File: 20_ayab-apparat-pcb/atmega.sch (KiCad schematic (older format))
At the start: 35 parts, among them P7 CONN_3X2, P8 CONN_4, P9 CONN_2, SW1 SW_PUSH, U6 ATMEGA32U4-A, X1 16MHz, X2 USBMINI

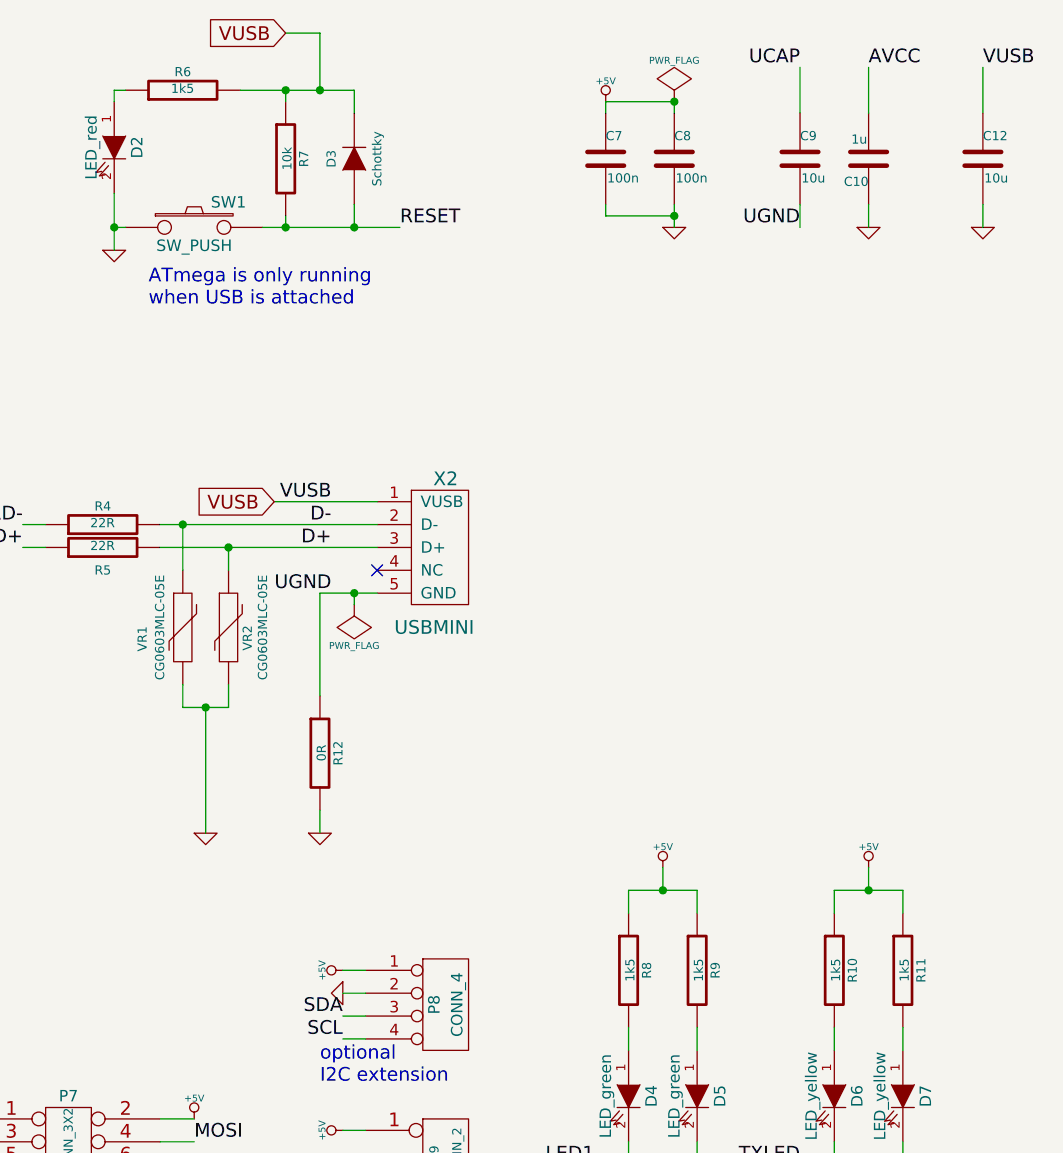
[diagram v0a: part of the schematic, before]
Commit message: fixed LED resistor value
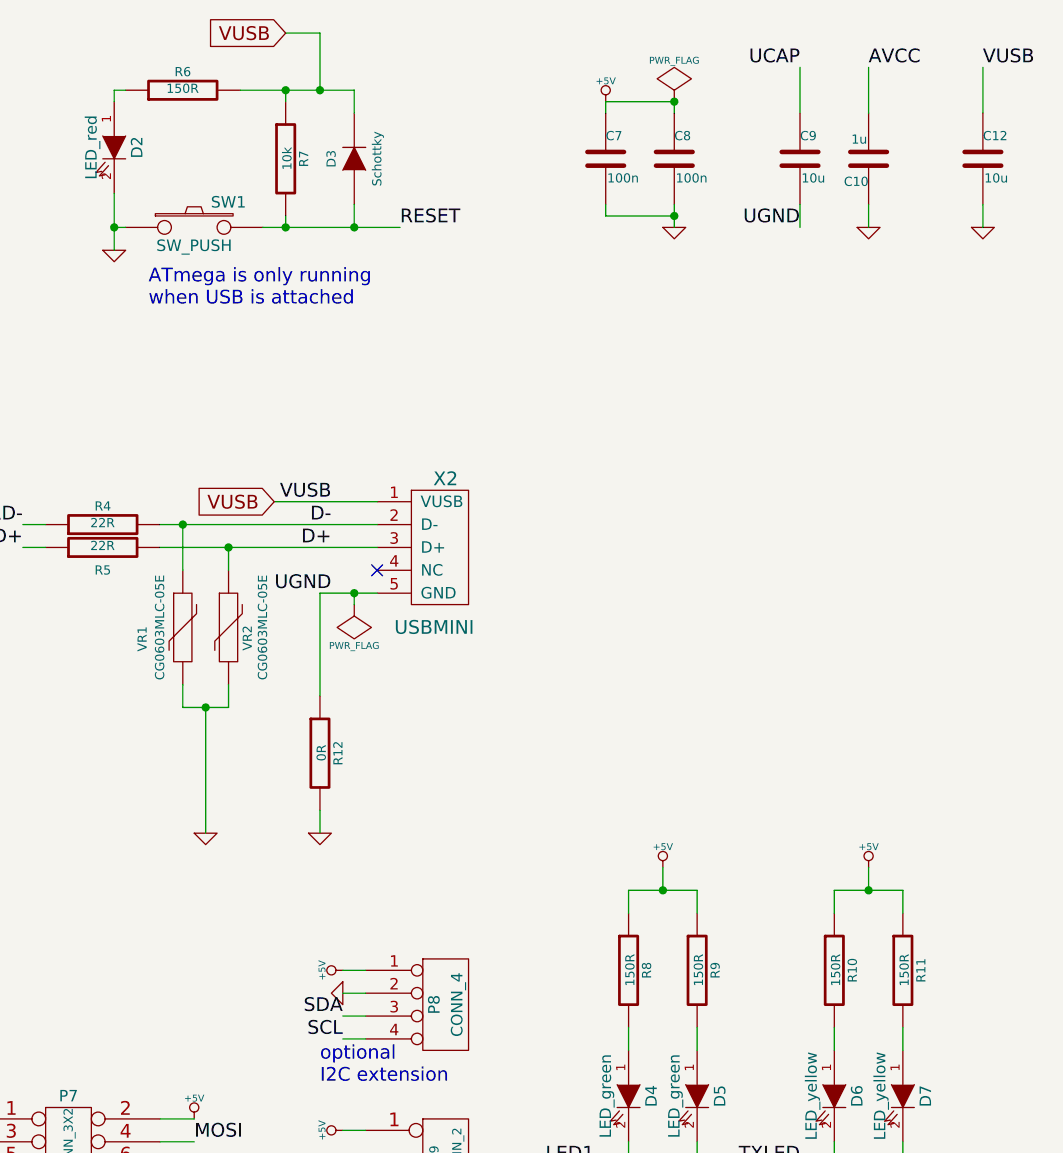
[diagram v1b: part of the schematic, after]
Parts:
- R10, R11, R6, R8, R9: value 1k5 -> 150R
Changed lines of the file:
@@
 OSC2
 $Comp
-L GND #PWR38
+L GND #PWR034
 U 1 1 52E8074E
 P 4750 1850
-F 0 "#PWR38" H 4750 1850 30  0001 C CNN
+F 0 "#PWR034" H 4750 1850 30  0001 C CNN
 F 1 "GND" H 4750 1780 30  0001 C CNN
 F 2 "" H 4750 1850 60  0000 C CNN
@@
 $EndComp
 $Comp
-L PWR_FLAG #FLG2
+L PWR_FLAG #FLG035
 U 1 1 52E8077D
 P 4750 1100
-F 0 "#FLG2" H 4750 1195 30  0001 C CNN
+F 0 "#FLG035" H 4750 1195 30  0001 C CNN
 F 1 "PWR_FLAG" H 4750 1280 30  0000 C CNN
 F 2 "" H 4750 1100 60  0000 C CNN
@@
 $EndComp
 $Comp
-L GND #PWR49
+L GND #PWR036
 U 1 1 52E80927
 P 9200 1700
-F 0 "#PWR49" H 9200 1700 30  0001 C CNN
+F 0 "#PWR036" H 9200 1700 30  0001 C CNN
 F 1 "GND" H 9200 1630 30  0001 C CNN
 F 2 "" H 9200 1700 60  0000 C CNN
@@
 $EndComp
 $Comp
-L PWR_FLAG #FLG4
+L PWR_FLAG #FLG037
 U 1 1 52E809A6
 P 9200 1150
-F 0 "#FLG4" H 9200 1245 30  0001 C CNN
+F 0 "#FLG037" H 9200 1245 30  0001 C CNN
 F 1 "PWR_FLAG" H 9200 1330 30  0000 C CNN
 F 2 "" H 9200 1150 60  0000 C CNN
@@
 $EndComp
 $Comp
-L GND #PWR34
+L GND #PWR038
 U 1 1 52E80AA1
 P 1450 5850
-F 0 "#PWR34" H 1450 5850 30  0001 C CNN
+F 0 "#PWR038" H 1450 5850 30  0001 C CNN
 F 1 "GND" H 1450 5780 30  0001 C CNN
 F 2 "" H 1450 5850 60  0000 C CNN
@@
 ISP
 $Comp
-L GND #PWR41
+L GND #PWR039
 U 1 1 52E80DFA
 P 7100 5850
-F 0 "#PWR41" H 7100 5850 30  0001 C CNN
+F 0 "#PWR039" H 7100 5850 30  0001 C CNN
 F 1 "GND" H 7100 5780 30  0001 C CNN
 F 2 "" H 7100 5850 60  0000 C CNN
@@
 MOSI
 $Comp
-L +5V #PWR40
+L +5V #PWR040
 U 1 1 52E80E45
 P 7100 5600
-F 0 "#PWR40" H 7100 5690 20  0001 C CNN
+F 0 "#PWR040" H 7100 5690 20  0001 C CNN
 F 1 "+5V" H 7100 5690 30  0000 C CNN
 F 2 "" H 7100 5600 60  0000 C CNN
@@
 P 7050 1100
 F 0 "R6" V 7130 1100 40  0000 C CNN
-F 1 "1k5" V 7057 1101 40  0000 C CNN
+F 1 "150R" V 7057 1101 40  0000 C CNN
 F 2 "" V 6980 1100 30  0000 C CNN
 F 3 "" H 7050 1100 30  0000 C CNN
@@
 $EndComp
 $Comp
-L GND #PWR39
+L GND #PWR041
 U 1 1 52E813A7
 P 6750 1800
-F 0 "#PWR39" H 6750 1800 30  0001 C CNN
+F 0 "#PWR041" H 6750 1800 30  0001 C CNN
 F 1 "GND" H 6750 1730 30  0001 C CNN
 F 2 "" H 6750 1800 60  0000 C CNN
@@
 $EndComp
 $Comp
-L +5V #PWR37
+L +5V #PWR042
 U 1 1 52E81906
 P 4350 3500
-F 0 "#PWR37" H 4350 3590 20  0001 C CNN
+F 0 "#PWR042" H 4350 3590 20  0001 C CNN
 F 1 "+5V" H 4350 3590 30  0000 C CNN
 F 2 "" H 4350 3500 60  0000 C CNN
@@
 $EndComp
 $Comp
-L +5V #PWR33
+L +5V #PWR043
 U 1 1 52E81C3C
 P 1300 5300
-F 0 "#PWR33" H 1300 5390 20  0001 C CNN
+F 0 "#PWR043" H 1300 5390 20  0001 C CNN
 F 1 "+5V" H 1300 5390 30  0000 C CNN
 F 2 "" H 1300 5300 60  0000 C CNN
@@
 RESET
 $Comp
-L GND #PWR35
+L GND #PWR044
 U 1 1 52E9637A
 P 2900 6200
-F 0 "#PWR35" H 2900 6200 30  0001 C CNN
+F 0 "#PWR044" H 2900 6200 30  0001 C CNN
 F 1 "GND" H 2900 6130 30  0001 C CNN
 F 2 "" H 2900 6200 60  0000 C CNN
@@
 $EndComp
 $Comp
-L GND #PWR42
+L GND #PWR045
 U 1 1 52E97A05
 P 7150 4350
-F 0 "#PWR42" H 7150 4350 30  0001 C CNN
+F 0 "#PWR045" H 7150 4350 30  0001 C CNN
 F 1 "GND" H 7150 4280 30  0001 C CNN
 F 2 "" H 7150 4350 60  0000 C CNN
@@
 $EndComp
 $Comp
-L GND #PWR50
+L GND #PWR046
 U 1 1 52E97015
 P 10050 1700
-F 0 "#PWR50" H 10050 1700 30  0001 C CNN
+F 0 "#PWR046" H 10050 1700 30  0001 C CNN
 F 1 "GND" H 10050 1630 30  0001 C CNN
 F 2 "" H 10050 1700 60  0000 C CNN
@@
 $EndComp
 $Comp
-L GND #PWR52
+L GND #PWR047
 U 1 1 52E972FE
 P 10550 1700
-F 0 "#PWR52" H 10550 1700 30  0001 C CNN
+F 0 "#PWR047" H 10550 1700 30  0001 C CNN
 F 1 "GND" H 10550 1630 30  0001 C CNN
 F 2 "" H 10550 1700 60  0000 C CNN
@@
 RXLED
 $Comp
-L +5V #PWR51
+L +5V #PWR048
 U 1 1 52E980C3
 P 10050 4500
-F 0 "#PWR51" H 10050 4590 20  0001 C CNN
+F 0 "#PWR048" H 10050 4590 20  0001 C CNN
 F 1 "+5V" H 10050 4590 30  0000 C CNN
 F 2 "" H 10050 4500 60  0000 C CNN
@@
 P 9900 4950
 F 0 "R10" V 9980 4950 40  0000 C CNN
-F 1 "1k5" V 9907 4951 40  0000 C CNN
+F 1 "150R" V 9907 4951 40  0000 C CNN
 F 2 "" V 9830 4950 30  0000 C CNN
 F 3 "" H 9900 4950 30  0000 C CNN
@@
 P 10200 4950
 F 0 "R11" V 10280 4950 40  0000 C CNN
-F 1 "1k5" V 10207 4951 40  0000 C CNN
+F 1 "150R" V 10207 4951 40  0000 C CNN
 F 2 "" V 10130 4950 30  0000 C CNN
 F 3 "" H 10200 4950 30  0000 C CNN
@@
 $EndComp
 $Comp
-L +5V #PWR46
+L +5V #PWR049
 U 1 1 52EA92E6
 P 7750 5650
-F 0 "#PWR46" H 7750 5740 20  0001 C CNN
+F 0 "#PWR049" H 7750 5740 20  0001 C CNN
 F 1 "+5V" H 7750 5740 30  0000 C CNN
 F 2 "" H 7750 5650 60  0000 C CNN
@@
 $EndComp
 $Comp
-L +5V #PWR44
+L +5V #PWR050
 U 1 1 52EA9766
 P 7750 4950
-F 0 "#PWR44" H 7750 5040 20  0001 C CNN
+F 0 "#PWR050" H 7750 5040 20  0001 C CNN
 F 1 "+5V" H 7750 5040 30  0000 C CNN
 F 2 "" H 7750 4950 60  0000 C CNN
@@
 $EndComp
 $Comp
-L GND #PWR45
+L GND #PWR051
 U 1 1 52EA977A
 P 7750 5050
-F 0 "#PWR45" H 7750 5050 30  0001 C CNN
+F 0 "#PWR051" H 7750 5050 30  0001 C CNN
 F 1 "GND" H 7750 4980 30  0001 C CNN
 F 2 "" H 7750 5050 60  0000 C CNN
@@
 LED2
 $Comp
-L +5V #PWR48
+L +5V #PWR052
 U 1 1 52EA9B0A
 P 9150 4500
-F 0 "#PWR48" H 9150 4590 20  0001 C CNN
+F 0 "#PWR052" H 9150 4590 20  0001 C CNN
 F 1 "+5V" H 9150 4590 30  0000 C CNN
 F 2 "" H 9150 4500 60  0000 C CNN
@@
 P 9000 4950
 F 0 "R8" V 9080 4950 40  0000 C CNN
-F 1 "1k5" V 9007 4951 40  0000 C CNN
+F 1 "150R" V 9007 4951 40  0000 C CNN
 F 2 "" V 8930 4950 30  0000 C CNN
 F 3 "" H 9000 4950 30  0000 C CNN
@@
 P 9300 4950
 F 0 "R9" V 9380 4950 40  0000 C CNN
-F 1 "1k5" V 9307 4951 40  0000 C CNN
+F 1 "150R" V 9307 4951 40  0000 C CNN
 F 2 "" V 9230 4950 30  0000 C CNN
 F 3 "" H 9300 4950 30  0000 C CNN
@@
 LED1
 $Comp
-L +5V #PWR36
+L +5V #PWR053
 U 1 1 52EAA0EE
 P 3050 2050
-F 0 "#PWR36" H 3050 2140 20  0001 C CNN
+F 0 "#PWR053" H 3050 2140 20  0001 C CNN
 F 1 "+5V" H 3050 2140 30  0000 C CNN
 F 2 "" H 3050 2050 60  0000 C CNN
@@
 $EndComp
 $Comp
-L +5V #PWR47
+L +5V #PWR054
 U 1 1 52EAA124
 P 8900 1150
-F 0 "#PWR47" H 8900 1240 20  0001 C CNN
+F 0 "#PWR054" H 8900 1240 20  0001 C CNN
 F 1 "+5V" H 8900 1240 30  0000 C CNN
 F 2 "" H 8900 1150 60  0000 C CNN
@@
 NoConn ~ 7900 3200
 $Comp
-L PWR_FLAG #FLG3
+L PWR_FLAG #FLG055
 U 1 1 52EECE74
 P 7800 3350
-F 0 "#FLG3" H 7800 3445 30  0001 C CNN
+F 0 "#FLG055" H 7800 3445 30  0001 C CNN
 F 1 "PWR_FLAG" H 7800 3530 30  0000 C CNN
 F 2 "" H 7800 3350 60  0000 C CNN
@@
 	7650 3750 7650 3300
 $Comp
-L GND #PWR43
+L GND #PWR056
 U 1 1 52F17DE8
 P 7650 4350
-F 0 "#PWR43" H 7650 4350 30  0001 C CNN
+F 0 "#PWR056" H 7650 4350 30  0001 C CNN
 F 1 "GND" H 7650 4280 30  0001 C CNN
 F 2 "" H 7650 4350 60  0000 C CNN

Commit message: ayab-apparat v2 ready for review
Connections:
- net +5V: no longer C7.1, C8.1
- net VUSB: now also C7.1, C8.1
